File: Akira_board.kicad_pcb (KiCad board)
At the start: 2 copper layers, 110 x 94 mm, 58 parts, among them SW1 Reset SW, SW2 Boot SW, Y1 16MHz

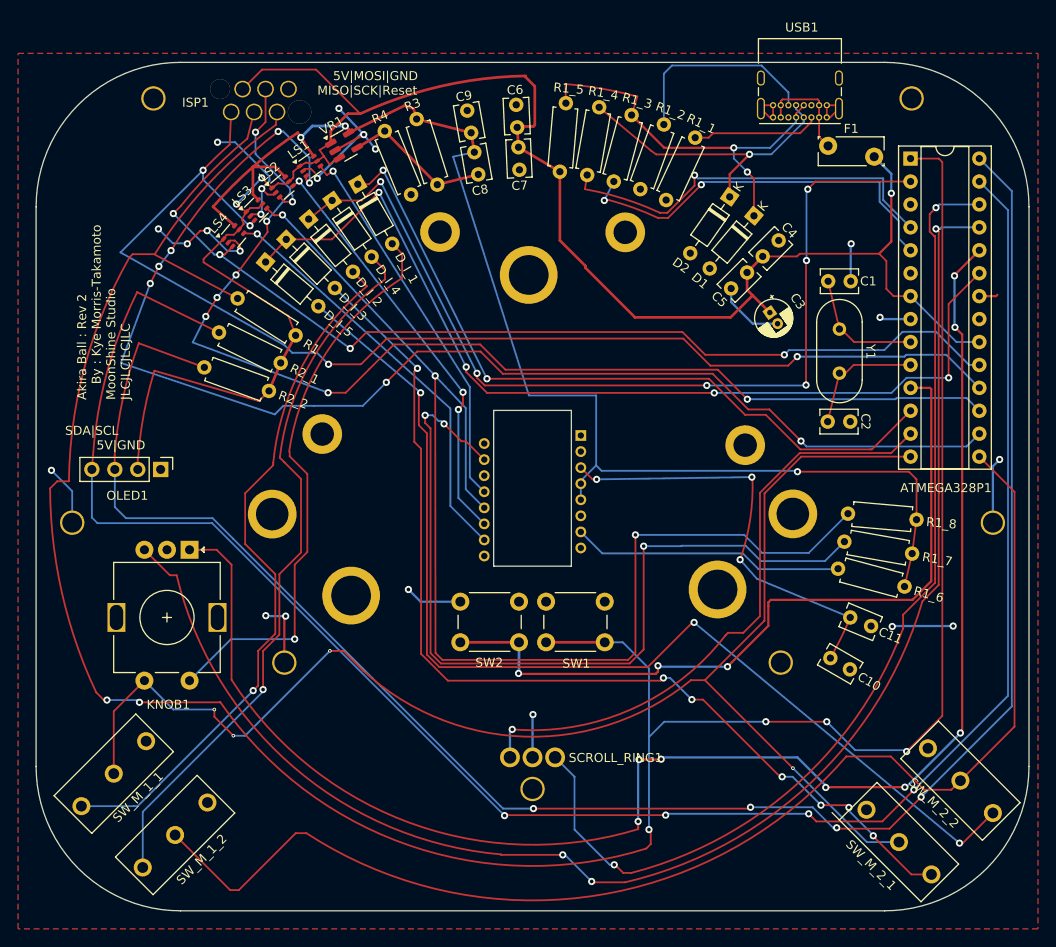
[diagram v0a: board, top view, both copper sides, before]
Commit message: fixed switch locations
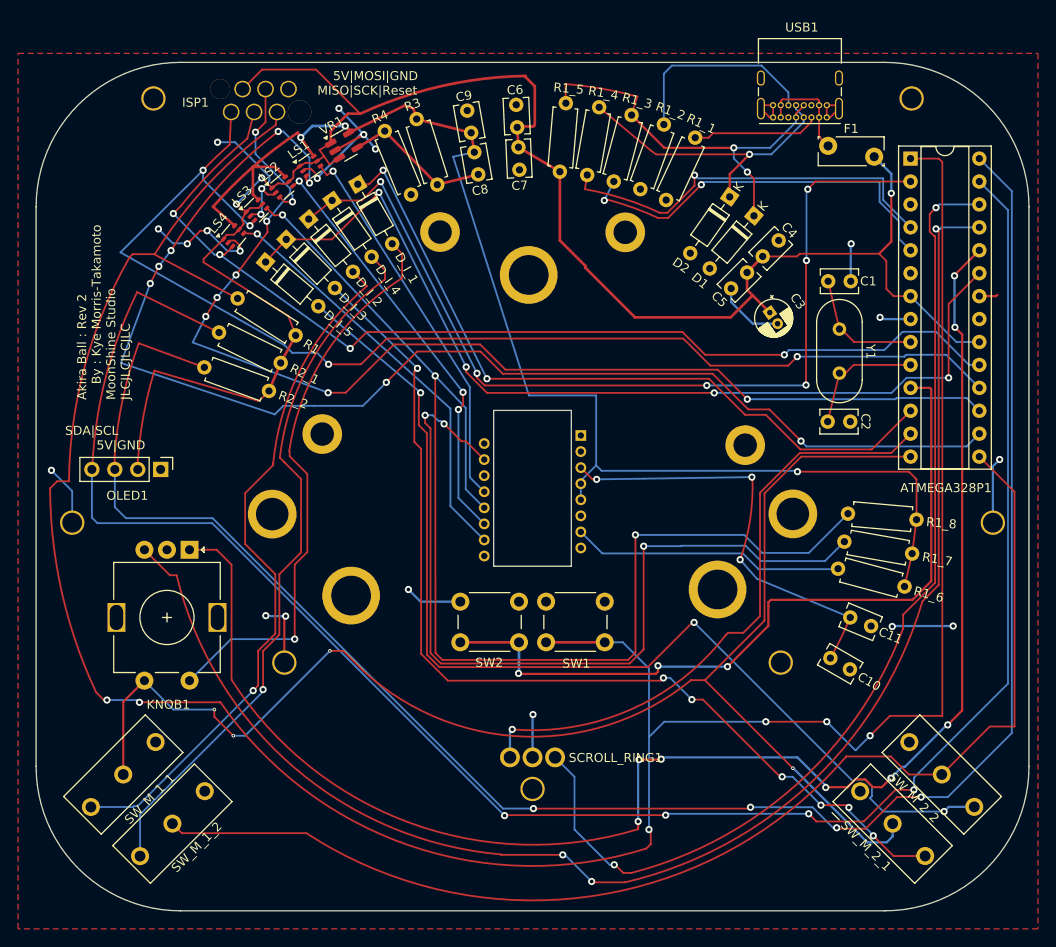
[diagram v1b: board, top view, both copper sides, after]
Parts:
- moved SW_M_2_1 8.89 mm to (189.9, 137.3)
- moved SW_M_2_2 8.86 mm to (195.3, 131.9)
- moved SW_M_1_1 8.83 mm to (104.7, 131.9)
- moved SW_M_1_2 8.54 mm to (110.1, 137.3)
- renumbered SW_M_1_2 to SW_M_1_1, SW_M_1_1 to SW_M_1_2, SW_M_2_2 to SW_M_2_1, SW_M_2_1 to SW_M_2_2
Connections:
- SW_M_1_1 pad COM: Net-(D_I_4-A) -> Net-(D_I_2-A)
- SW_M_1_1 pad NO: COL1 -> COL0
- SW_M_1_2 pad COM: Net-(D_I_2-A) -> Net-(D_I_4-A)
- SW_M_1_2 pad NO: COL0 -> COL1
- SW_M_2_1 pad COM: Net-(D_I_5-A) -> Net-(D_I_3-A)
- SW_M_2_1 pad NO: COL1 -> COL0
- SW_M_2_2 pad COM: Net-(D_I_3-A) -> Net-(D_I_5-A)
- SW_M_2_2 pad NO: COL0 -> COL1
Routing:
- net COL1: track 74.3 -> 68.5 mm
- net Net-(D_I_5-A): track 119.9 -> 117.7 mm
- net I2C_SCL: track 195.5 -> 197.2 mm
- net Net-(D_I_3-A): track 112.1 -> 110.5 mm
- net Net-(D_I_4-A): track 56.8 -> 55.6 mm
- net Net-(D_I_2-A): track 55.5 -> 54.5 mm
- net COL0: track 115.6 -> 116.2 mm
- net VK_A: track 120.9 -> 120.4 mm
